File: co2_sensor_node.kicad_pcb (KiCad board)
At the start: 4 copper layers, 52.5 x 96 mm, 77 parts, among them J1 Conn_01x07_Female, J10 Conn_01x02_Male, J11 Conn_01x02_Male, J12 Conn_01x02_Male, J13 Conn_01x02_Male, J14 Conn_01x02, J15 Conn_01x06_Male, J2 Conn_01x04_Female, J3 Conn_01x07_Female, J4 Conn_01x04_Female, J5 Conn_01x04_Female, J6 TF-15x15, J7 SMA Female, J8 Conn_01x02_Male, J9 Conn_01x02_Male, Q1 AO3400A, Q2 AO3401A, Q3 AO3400A, Q4 AO3401A, Q5 AO3401A, SW1 K2-1102SP-C4SC-04, U1 RFM95W-868S2, U2 ublox_SAM-M8Q, U3 TPS62130, U4 TPS62130, U5 ESP32-WROOM-32D

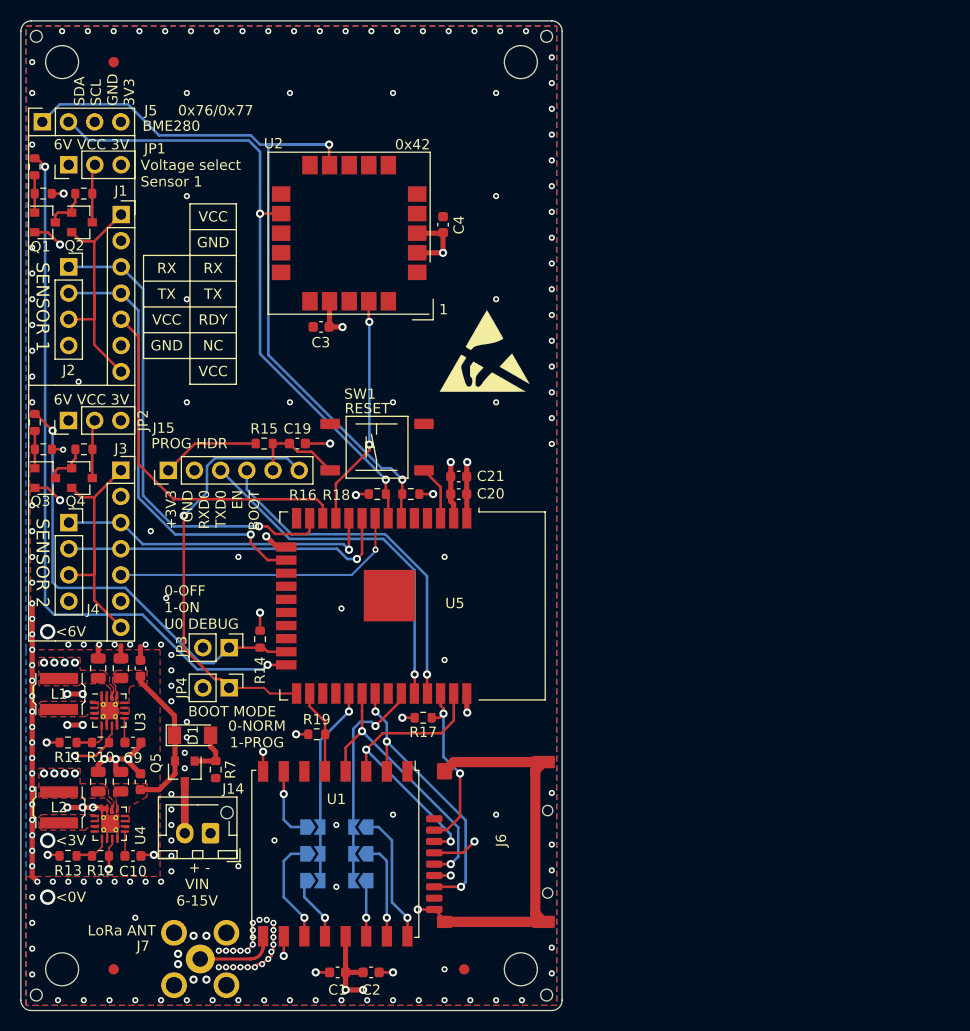
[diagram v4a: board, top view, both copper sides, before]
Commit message: Finish routing of Rev 1
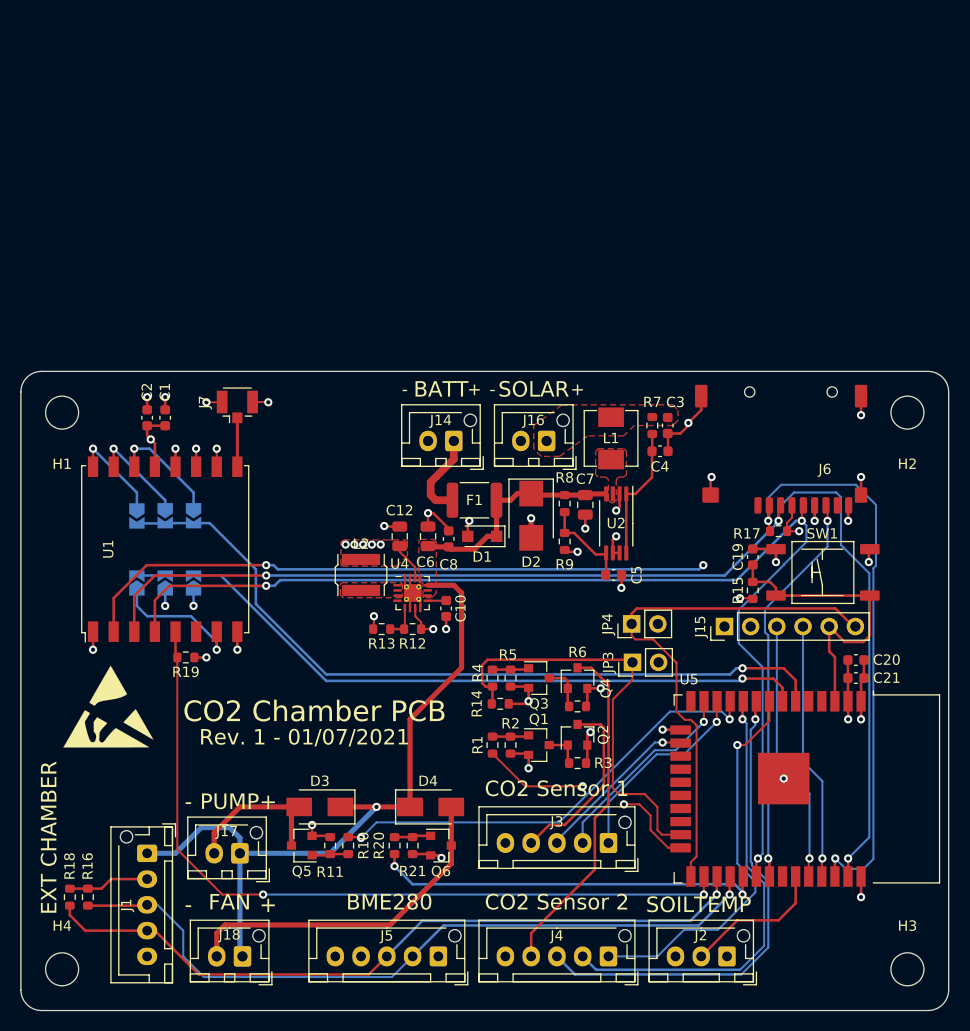
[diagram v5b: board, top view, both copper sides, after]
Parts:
- removed BOARD_FIDUCIAL (x3): Fiducial_1mm_Mask2mm, Fiducial:Fiducial_1mm_Mask2mm
- removed C11: 22u, Capacitor_SMD:C_0805_2012Metric
- removed C9: 3n3, Capacitor_SMD:C_0603_1608Metric
- removed JP1, JP2: PWR_JP, Connector_PinHeader_2.54mm:PinHeader_1x03_P2.54mm_Vertical
- removed the REF** at (171.5, 45.5)
- removed the REF** at (122.0, 138.5)
- removed the REF** at (122.0, 45.5)
- removed the REF** at (171.5, 138.5)
- removed U3: TPS62130, Package_DFN_QFN:VQFN-16-1EP_3x3mm_P0.5mm_EP1.68x1.68mm_ThermalVias
- added D2: P6SMB6.8CA, Diode_SMD:D_SMB, F.Cu at (170.0, 92.0)
- added D3: SS34, Diode_SMD:D_SMA, F.Cu at (149.5, 120.2)
- added D4: SS34, Diode_SMD:D_SMA, F.Cu at (160.2, 120.2)
- added F1: mSMD200-16V, Fuse:Fuse_1812_4532Metric, F.Cu at (164.5, 90.5)
- added J16: Conn_01x02, Connector_JST:JST_XH_B2B-XH-AM_1x02_P2.50mm_Vertical, F.Cu at (171.5, 84.8)
- added J17: Conn_01x02, Connector_JST:JST_XH_B2B-XH-AM_1x02_P2.50mm_Vertical, F.Cu at (141.8, 124.8)
- added J18: Conn_01x02, Connector_JST:JST_XH_B2B-XH-AM_1x02_P2.50mm_Vertical, F.Cu at (142.0, 134.8)
- added Q6: AO3400A, Package_TO_SOT_SMD:SOT-23, F.Cu at (161.2, 124.0)
- added R20: 220R, Resistor_SMD:R_0603_1608Metric, F.Cu at (156.8, 124.0)
- added R21: 10K, Resistor_SMD:R_0603_1608Metric, F.Cu at (158.5, 124.0)
- added R8: 820k, Resistor_SMD:R_0603_1608Metric, F.Cu at (173.2, 90.8)
- added R9: 360k, Resistor_SMD:R_0603_1608Metric, F.Cu at (173.2, 94.5)
- C4: value 100n -> 1n
- C5: value 10u -> 1n; footprint Capacitor_SMD:C_0805_2012Metric -> Capacitor_SMD:C_0603_1608Metric
- C7: value 100n -> 10u; footprint Capacitor_SMD:C_0603_1608Metric -> Capacitor_SMD:C_0805_2012Metric
- D1: value 5V6 -> SM4007PL; footprint Diode_SMD:D_MiniMELF -> Diode_SMD:D_SOD-123F
- J1, J3: value Conn_01x07_Female -> Conn_01x05; footprint Connector_PinSocket_2.54mm:PinSocket_1x07_P2.54mm_Vertical -> Connector_JST:JST_XH_B5B-XH-AM_1x05_P2.50mm_Vertical
- J2: value Conn_01x04_Female -> Conn_01x03; footprint Connector_PinSocket_2.54mm:PinSocket_1x04_P2.54mm_Vertical -> Connector_JST:JST_XH_B3B-XH-AM_1x03_P2.50mm_Vertical
- J4, J5: value Conn_01x04_Female -> Conn_01x05; footprint Connector_PinSocket_2.54mm:PinSocket_1x04_P2.54mm_Vertical -> Connector_JST:JST_XH_B5B-XH-AM_1x05_P2.50mm_Vertical
- J7: value SMA Female -> U.FL; footprint co2_sensor_node:TE_5-1814832-2_C482015 -> Connector_Coaxial:U.FL_Hirose_U.FL-R-SMT-1_Vertical
- L1: value 2u2 -> 10u; footprint co2_sensor_node:WPN4020 -> co2_sensor_node:MWSA0503S
- Q5: value AO3401A -> AO3400A
- R10: value 1M17 -> 220R
- R11: value 180k -> 10K
- R7: value 10k -> 1k
- U2: value ublox_SAM-M8Q -> SPV1040; footprint RF_GPS:ublox_SAM-M8Q -> Package_SO:TSSOP-8_4.4x3mm_P0.65mm
- moved J2 92.5 mm to (189.0, 134.8), turned to 180 degrees
- moved J5 89.6 mm to (161.0, 134.8), turned to 180 degrees
- moved H3 82.0 mm to (206.5, 136.0)
- moved R3 73.1 mm to (174.5, 116.0)
- moved R1 71.5 mm to (166.2, 114.2), turned to 90 degrees
- moved R2 70.1 mm to (168.0, 114.2), turned to 270 degrees
- moved Q1 69.8 mm to (170.8, 114.2)
- moved Q2 69.1 mm to (174.5, 113.2), turned to 90 degrees
- moved J4 67.2 mm to (177.5, 134.8), turned to 180 degrees
- moved J1 62.0 mm to (132.8, 124.8), turned to 270 degrees
- moved L1 59.7 mm to (177.8, 84.5), turned to 270 degrees
- moved J3 59.5 mm to (177.5, 123.8), turned to 180 degrees
- moved C2 58.0 mm to (132.8, 82.5), turned to 90 degrees
- moved C1 56.3 mm to (134.5, 82.5), turned to 90 degrees
- moved J15 56.0 mm to (188.8, 102.8)
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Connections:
- C3 pad 1: +3V3 -> Net-(C3-Pad1)
- C4 pad 1: +3V3 -> Net-(C4-Pad1)
- C5 pad 1: +BATT -> Net-(C5-Pad1)
- D1 pad 2: Net-(D1-Pad2) -> GND
- J1 pad 1: /CO2 Sensor Connector 1/VCC -> +BATT
- J1 pad 2: GND -> +3V3
- J1 pad 3: /Microprocessor section/UART1_RX -> /Microprocessor section/I2C_SCL
- J1 pad 4: /Microprocessor section/UART1_TX -> /Microprocessor section/I2C_SDA
- J1 pad 5: /CO2 Sensor Connector 1/N_RDY -> GND
- J14 pad 1: GND -> Net-(F1-Pad2)
- J14 pad 2: Net-(J14-Pad2) -> GND
- J2 pad 1: /Microprocessor section/UART1_RX -> +3V3
- J2 pad 2: /Microprocessor section/UART1_TX -> /Microprocessor section/TEMPSENSOR
- J2 pad 3: /CO2 Sensor Connector 1/VCC -> GND
- J3 pad 1: /CO2 Sensor Connector 2/VCC -> /CO2 Sensor Connector 1/N_RDY
- J3 pad 2: GND -> /Microprocessor section/UART1_RX
- J3 pad 3: /Microprocessor section/UART2_RX -> /Microprocessor section/UART1_TX
- J3 pad 4: /Microprocessor section/UART2_TX -> /CO2 Sensor Connector 1/VCC
- J3 pad 5: /CO2 Sensor Connector 2/N_RDY -> GND
- J4 pad 1: /Microprocessor section/UART2_RX -> /CO2 Sensor Connector 2/N_RDY
- J4 pad 2: /Microprocessor section/UART2_TX -> /Microprocessor section/UART2_RX
- J4 pad 3: /CO2 Sensor Connector 2/VCC -> /Microprocessor section/UART2_TX
- J4 pad 4: GND -> /CO2 Sensor Connector 2/VCC
- J5 pad 1: /Microprocessor section/I2C_SDA -> +3V3
- J5 pad 3: GND -> /Microprocessor section/I2C_SDA
- J5 pad 4: +3V3 -> GND
- L1 pad 1: Net-(L1-Pad1) -> Net-(C3-Pad1)
- L1 pad 2: +6V -> Net-(L1-Pad2)
- Q2 pad 2: /CO2 Sensor Connector 1/VCC -> +3V3
- Q2 pad 3: Net-(JP1-Pad2) -> /CO2 Sensor Connector 1/VCC
- Q4 pad 2: /CO2 Sensor Connector 2/VCC -> +3V3
- Q4 pad 3: Net-(JP2-Pad2) -> /CO2 Sensor Connector 2/VCC
- Q5 pad 1: Net-(D1-Pad2) -> Net-(Q5-Pad1)
- Q5 pad 2: +BATT -> GND
- Q5 pad 3: Net-(J14-Pad2) -> Net-(D3-Pad2)
- R10 pad 1: +6V -> Net-(Q5-Pad1)
- R10 pad 2: Net-(R10-Pad2) -> /Microprocessor section/PUMP_EN
- R11 pad 1: Net-(R10-Pad2) -> Net-(Q5-Pad1)
- R3 pad 1: Net-(JP1-Pad2) -> +3V3
- R6 pad 1: Net-(JP2-Pad2) -> +3V3
- R7 pad 1: Net-(D1-Pad2) -> Net-(C3-Pad1)
- R7 pad 2: GND -> Net-(C4-Pad1)
- U2 pad 1: GND -> Net-(C4-Pad1)
- U2 pad 2: +3V3 -> GND
- U2 pad 3: +3V3 -> Net-(L1-Pad2)
- U2 pad 4: GND -> +BATT
- U2 pad 5: GND -> Net-(C5-Pad1)
- U2 pad 7: Net-(U2-Pad7) -> GND
- U2 pad 8: Net-(U2-Pad8) -> Net-(C4-Pad1)
- U5 pad 11: /GNSS/ENABLE -> /Microprocessor section/PUMP_EN
- U5 pad 27: Net-(U5-Pad27) -> /Microprocessor section/I2C_SDA
- U5 pad 28: Net-(U5-Pad28) -> /Microprocessor section/I2C_SCL
- U5 pad 29: /LoRa Transceiver/IRQ1 -> /Fan/FAN
- U5 pad 33: /LoRa Transceiver/IRQ2 -> /Microprocessor section/TEMPSENSOR
- U5 pad 6: /Microprocessor section/I2C_SDA -> /LoRa Transceiver/IRQ2
- U5 pad 7: /Microprocessor section/I2C_SCL -> /LoRa Transceiver/IRQ1
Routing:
- net /LoRa Transceiver/MOSI: track 28.3 -> 117.5 mm, vias 2 -> 3
- net /LoRa Transceiver/MISO: track 28.1 -> 115.4 mm, vias 3 -> 4
- net /LoRa Transceiver/SCLK: track 26.9 -> 109.2 mm, vias 2 -> 3
- net +BATT: track 14.8 -> 92.5 mm, vias 0 -> 1
- net +6V: track 72.5 -> 0.00 mm, vias 6 -> 0
- net /LoRa Transceiver/CSN: track 8.16 -> 75.8 mm, vias 0 -> 2
- net GND: track 144.2 -> 81.5 mm, vias 207 -> 34
- net /LoRa Transceiver/IRQ2: track 21.5 -> 74.7 mm
- net /LoRa Transceiver/IRQ1: track 19.3 -> 68.6 mm
- net /CO2 Sensor Connector 1/ENABLE: track 70.1 -> 22.9 mm
- net /Microprocessor section/PUMP_EN: track 0.00 -> 44.2 mm, vias 0 -> 2
- net /SD Card/CSN: track 17.1 -> 57.3 mm
- net /Fan/FAN: track 0.00 -> 38.0 mm, vias 0 -> 2
- net Net-(D4-Pad2): track 0.00 -> 33.1 mm
- net /Microprocessor section/UART1_RX: track 47.2 -> 19.8 mm
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- added copper zone on F.Cu, net Net-(C3-Pad1)
- added copper zone on F.Cu, net Net-(L1-Pad2)
- removed copper zone on F.Cu, net +6V
- removed copper zone on B.Cu, net GND
- removed copper zone on F.Cu, net GND
- removed copper zone on F.Cu, net Net-(L1-Pad1)
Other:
- board size 52.5 x 96 mm -> 90 x 62 mm
- board text added: "+"
- board text added: "-"
- board text added: "BATT"
- board text added: "CO2 Chamber PCB"
- board text added: "CO2 Sensor 1"
- board text added: "CO2 Sensor 2"
- board text added: "EXT CHAMBER"
- board text added: "FAN"
- board text added: "PUMP"
- board text added: "Rev. 1 - 01/07/2021"
- board text added: "SOILTEMP"
- board text added: "SOLAR"
- board text removed: "+ - VIN 6-15V"
- board text removed: "+3V3 GND RXD0 TXD0 EN BOOT"
- board text removed: "0-NORM 1-PROG"
- board text removed: "0-OFF 1-ON U0 DEBUG"
- board text removed: "0x42"
- board text removed: "0x76/0x77"
- board text removed: "1"
- board text removed: "6V VCC 3V"
- board text removed: "<0V"
- board text removed: "<3V"
- board text removed: "<6V"
- board text removed: "BOARD STACKUP: JLC7628"
- board text removed: "BOOT MODE"
- board text removed: "DIO2 DIO1 DIO0"
- board text removed: "DIO5 DIO3 DIO4"
- board text removed: "GND"
- board text removed: "IRQ1"
- board text removed: "IRQ2"
- board text removed: "LoRa ANT"
- board text removed: "NC"
- board text removed: "RDY"
- board text removed: "RESET"
- board text removed: "RX"
- board text removed: "SDA SCL GND 3V3"
- board text removed: "SENSOR 1"
- board text removed: "SENSOR 2"
- board text removed: "TX"
- board text removed: "VCC"
- board text removed: "Voltage select Sensor 1"

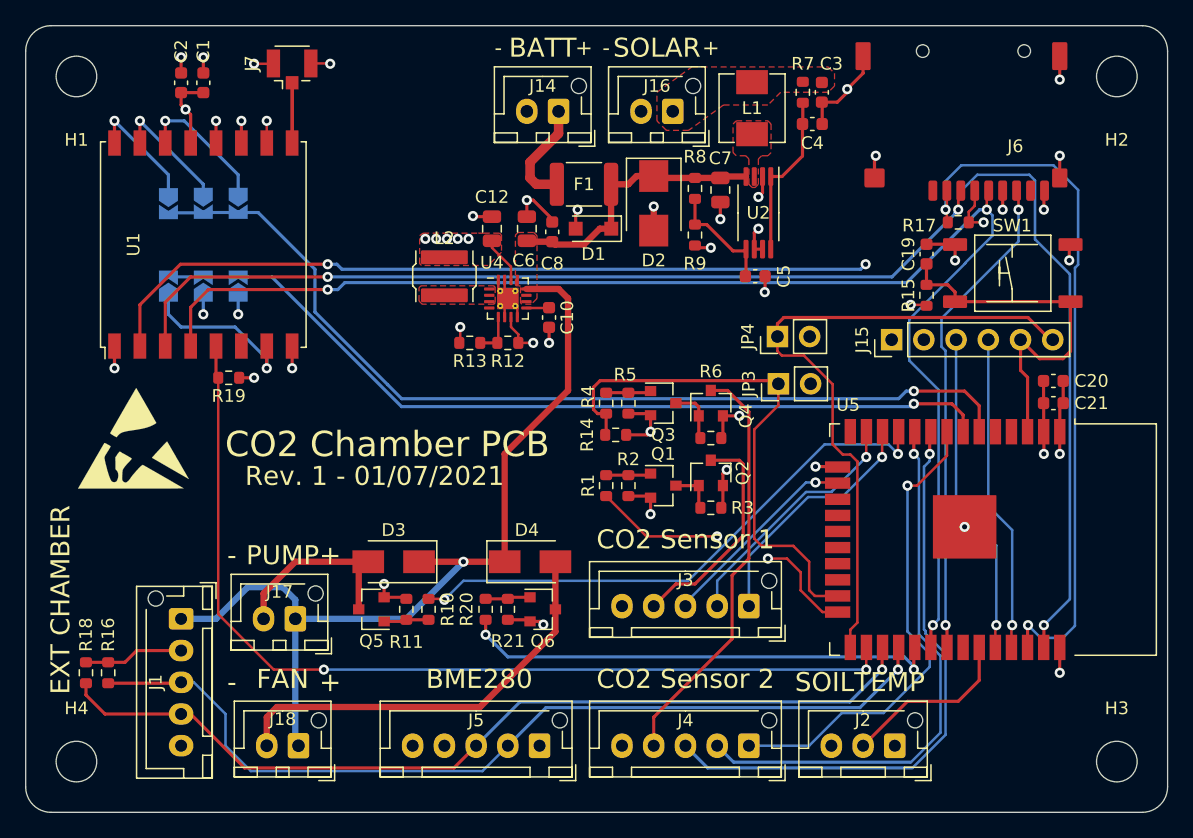
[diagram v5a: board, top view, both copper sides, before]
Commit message: Remove unused circuits
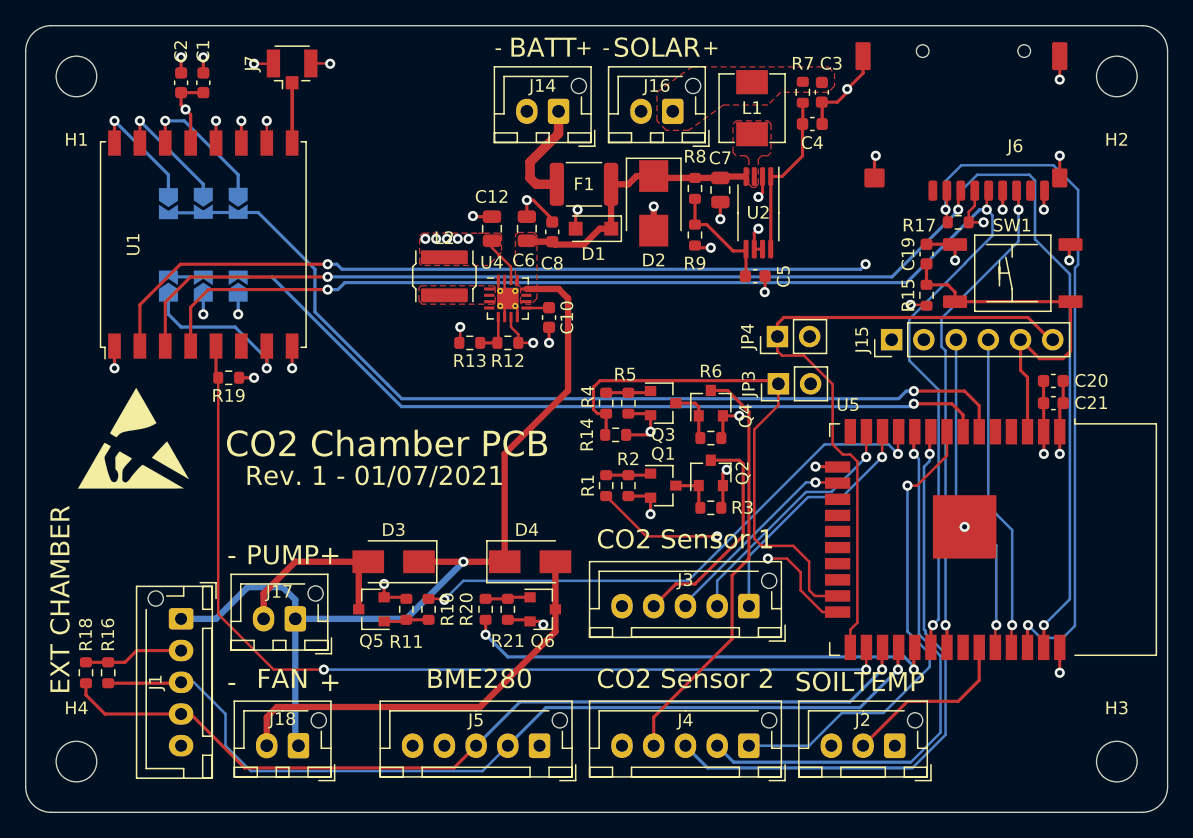
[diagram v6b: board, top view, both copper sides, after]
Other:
- net class Default removed

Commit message: Finalize schematic
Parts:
- removed C19, C21: 100n, Capacitor_SMD:C_0603_1608Metric
- removed C20: 1u, Capacitor_SMD:C_0603_1608Metric
- removed D4: SS34, Diode_SMD:D_SMA
- removed J14, J16, J17, J18: Conn_01x02, Connector_JST:JST_XH_B2B-XH-AM_1x02_P2.50mm_Vertical
- removed J15: Conn_01x06_Male, Connector_PinHeader_2.54mm:PinHeader_1x06_P2.54mm_Vertical
- removed JP3: MTDO_JP, Connector_PinHeader_2.54mm:PinHeader_1x02_P2.54mm_Vertical
- removed JP4: BOOT_JP, Connector_PinHeader_2.54mm:PinHeader_1x02_P2.54mm_Vertical
- removed L2: 2u2, co2_sensor_node:WPN4020
- removed Q5, Q6: AO3400A, Package_TO_SOT_SMD:SOT-23
- removed R17, R19: 10k, Resistor_SMD:R_0603_1608Metric
- removed R18: 4k7, Resistor_SMD:R_0603_1608Metric
- removed R20: 220R, Resistor_SMD:R_0603_1608Metric
- removed R21: 10K, Resistor_SMD:R_0603_1608Metric
- removed REF**: ESD-Logo_8.9x8mm_SilkScreen, Symbol:ESD-Logo_8.9x8mm_SilkScreen
- removed U4: TPS62130, Package_DFN_QFN:VQFN-16-1EP_3x3mm_P0.5mm_EP1.68x1.68mm_ThermalVias
- removed U5: ESP32-WROOM-32D, RF_Module:ESP32-WROOM-32
- added C11: 10u, Capacitor_SMD:C_0805_2012Metric, F.Cu at (210.5, 99.8)
- added C9: 100n, Capacitor_SMD:C_0603_1608Metric, F.Cu at (117.7, 55.7)
- added JP1: MTDO_JP, Connector_PinHeader_2.54mm:PinHeader_1x02_P2.54mm_Vertical, F.Cu at (113.3, 56.8)
- added JP2: BOOT_JP, Connector_PinHeader_2.54mm:PinHeader_1x02_P2.54mm_Vertical, F.Cu at (108.7, 81.2)
- added TP1: 3V3_Switched, TestPoint:TestPoint_Loop_D2.50mm_Drill1.0mm_LowProfile, F.Cu at (106.9, 115.3)
- added TP10: GND, TestPoint:TestPoint_Loop_D2.50mm_Drill1.0mm_LowProfile, F.Cu at (118.3, 106.9)
- added TP11: GND, TestPoint:TestPoint_Loop_D2.50mm_Drill1.0mm_LowProfile, F.Cu at (125.5, 102.3)
- added TP12: TEMP_SENSOR, TestPoint:TestPoint_Loop_D2.50mm_Drill1.0mm_LowProfile, F.Cu at (106.9, 119.9)
- added TP13: MOISTURE_SENSOR, TestPoint:TestPoint_Loop_D2.50mm_Drill1.0mm_LowProfile, F.Cu at (113.7, 110.2)
- added TP14: CELL_1, TestPoint:TestPoint_Loop_D2.50mm_Drill1.0mm_LowProfile, F.Cu at (216.3, 62.1)
- added TP15: CELL_2, TestPoint:TestPoint_Loop_D2.50mm_Drill1.0mm_LowProfile, F.Cu at (225.9, 56.8)
- added TP16: VALVE_1_REV, TestPoint:TestPoint_Loop_D2.50mm_Drill1.0mm_LowProfile, F.Cu at (200.8, 112.3)
- added TP17: VALVE_2_FWD, TestPoint:TestPoint_Loop_D2.50mm_Drill1.0mm_LowProfile, F.Cu at (209.4, 96.0)
- added TP18: VALVE_1_FWD, TestPoint:TestPoint_Loop_D2.50mm_Drill1.0mm_LowProfile, F.Cu at (209.4, 91.3)
- added TP19: VALVE_2_REV, TestPoint:TestPoint_Loop_D2.50mm_Drill1.0mm_LowProfile, F.Cu at (214.0, 91.3)
- added TP2: SCL, TestPoint:TestPoint_Loop_D2.50mm_Drill1.0mm_LowProfile, F.Cu at (120.9, 97.6)
- added TP20: MOSI, TestPoint:TestPoint_Loop_D2.50mm_Drill1.0mm_LowProfile, F.Cu at (170.2, 70.3)
- added TP21: SCLK, TestPoint:TestPoint_Loop_D2.50mm_Drill1.0mm_LowProfile, F.Cu at (174.8, 70.3)
- added TP22: SD_CSN, TestPoint:TestPoint_Loop_D2.50mm_Drill1.0mm_LowProfile, F.Cu at (187.9, 56.8)
- added TP23: MISO, TestPoint:TestPoint_Loop_D2.50mm_Drill1.0mm_LowProfile, F.Cu at (170.2, 74.9)
- added TP3: SDA, TestPoint:TestPoint_Loop_D2.50mm_Drill1.0mm_LowProfile, F.Cu at (112.9, 105.6)
- added TP4: 3V3, TestPoint:TestPoint_Loop_D2.50mm_Drill1.0mm_LowProfile, F.Cu at (123.0, 106.9)
- added TP5: PWR_EN, TestPoint:TestPoint_Loop_D2.50mm_Drill1.0mm_LowProfile, F.Cu at (109.0, 110.2)
- added TP6: CO2_RX, TestPoint:TestPoint_Loop_D2.50mm_Drill1.0mm_LowProfile, F.Cu at (111.6, 114.9)
- added TP7: CO2_TX, TestPoint:TestPoint_Loop_D2.50mm_Drill1.0mm_LowProfile, F.Cu at (118.3, 111.6)
- added TP8: GND, TestPoint:TestPoint_Loop_D2.50mm_Drill1.0mm_LowProfile, F.Cu at (125.5, 97.6)
- added TP9: GND, TestPoint:TestPoint_Loop_D2.50mm_Drill1.0mm_LowProfile, F.Cu at (120.9, 102.3)
- added U3: TC1508S, Package_SO:SOP-16_3.9x9.9mm_P1.27mm, F.Cu at (202.8, 94.7)
- C1: value 1u -> 10u; footprint Capacitor_SMD:C_0603_1608Metric -> Capacitor_SMD:C_0805_2012Metric
- C10: value 3n3 -> 220u; footprint Capacitor_SMD:C_0603_1608Metric -> Capacitor_THT:CP_Radial_D8.0mm_P3.50mm
- C12: value 22u -> 100n; footprint Capacitor_SMD:C_0805_2012Metric -> Capacitor_SMD:C_0603_1608Metric
- C3: value 1u -> 3n3
- C4, C5: value 1n -> 1u
- C6: value 10u -> 22u
- C7: value 10u -> 100n; footprint Capacitor_SMD:C_0805_2012Metric -> Capacitor_SMD:C_0603_1608Metric
- C8: value 100n -> 1u
- D1: value SM4007PL -> Green LED; footprint Diode_SMD:D_SOD-123F -> LED_SMD:LED_0603_1608Metric
- D2: value P6SMB6.8CA -> ZMM5V6-M; footprint Diode_SMD:D_SMB -> Diode_SMD:D_MiniMELF
- J1: value Conn_01x05 -> Conn_01x03; footprint Connector_JST:JST_XH_B5B-XH-AM_1x05_P2.50mm_Vertical -> Connector_PinSocket_2.54mm:PinSocket_1x03_P2.54mm_Vertical
- J10, J9: value Conn_01x02_Male -> Conn_01x05; footprint Jumper:SolderJumper-2_P1.3mm_Open_TrianglePad1.0x1.5mm -> Connector_JST:JST_XH_B5B-XH-AM_1x05_P2.50mm_Vertical; moved to F.Cu
- J11: value Conn_01x02_Male -> Conn_01x06_Male; footprint Jumper:SolderJumper-2_P1.3mm_Open_TrianglePad1.0x1.5mm -> Connector_PinHeader_2.54mm:PinHeader_1x06_P2.54mm_Vertical; moved to F.Cu
- J12: value Conn_01x02_Male -> Conn_01x02; footprint Jumper:SolderJumper-2_P1.3mm_Open_TrianglePad1.0x1.5mm -> co2_sensor_node:KF301-5.0-2P; moved to F.Cu
- J13: value Conn_01x02_Male -> TF-15x15; footprint Jumper:SolderJumper-2_P1.3mm_Open_TrianglePad1.0x1.5mm -> co2_sensor_node:TF-15x15; moved to F.Cu
- J2: footprint Connector_JST:JST_XH_B3B-XH-AM_1x03_P2.50mm_Vertical -> Connector_PinSocket_2.54mm:PinSocket_1x03_P2.54mm_Vertical
- J3, J4: value Conn_01x05 -> Conn_01x02; footprint Connector_JST:JST_XH_B5B-XH-AM_1x05_P2.50mm_Vertical -> co2_sensor_node:KF301-5.0-2P
- J5: value Conn_01x05 -> Conn_01x03; footprint Connector_JST:JST_XH_B5B-XH-AM_1x05_P2.50mm_Vertical -> co2_sensor_node:KF301-5.0-3P
- J6: value TF-15x15 -> Conn_01x03; footprint co2_sensor_node:TF-15x15 -> co2_sensor_node:KF301-5.0-3P
- J7: value U.FL -> Conn_01x02; footprint Connector_Coaxial:U.FL_Hirose_U.FL-R-SMT-1_Vertical -> Connector_JST:JST_XH_B2B-XH-AM_1x02_P2.50mm_Vertical
- J8: value Conn_01x02_Male -> Conn_01x03; footprint Jumper:SolderJumper-2_P1.3mm_Open_TrianglePad1.0x1.5mm -> Connector_JST:JST_XH_B3B-XH-AM_1x03_P2.50mm_Vertical; moved to F.Cu
- L1: value 10u -> 2u2; footprint co2_sensor_node:MWSA0503S -> co2_sensor_node:WPN4020
- Q3: value AO3400A -> AO3401A
- Q4: value AO3401A -> AO3400A
- R1: value 220 -> 4k7
- R10: value 220R -> 562k
- R11: value 10K -> 180k
- R12: value 562k -> 10k
- R13: value 180k -> 10k
- R14: value 10k -> 220R
- R15: value 10k -> 10K
- R16: value 4k7 -> 10k
- R2: value 10k -> 4k7
- R3: value 10k -> 1k
- R7: value 1k -> 220
- R8: value 820k -> 220
- R9: value 360k -> 1M
- U1: value RFM95W-868S2 -> TPS62130; footprint RF_Module:HOPERF_RFM9XW_SMD -> Package_DFN_QFN:VQFN-16-1EP_3x3mm_P0.5mm_EP1.68x1.68mm_ThermalVias
- U2: value SPV1040 -> ESP32-WROOM-32D; footprint Package_SO:TSSOP-8_4.4x3mm_P0.65mm -> RF_Module:ESP32-WROOM-32
- moved J6 112.2 mm to (80.2, 99.8), turned to 0 degrees
- moved H3 107.3 mm to (102.7, 109.0)
- moved J3 97.5 mm to (80.2, 118.4), turned to 0 degrees
- moved C7 96.4 mm to (78.8, 90.8), turned to 0 degrees
- moved U1 94.5 mm to (220.9, 57.1), turned to 0 degrees
- moved H2 93.5 mm to (114.6, 99.3)
- moved R3 92.0 mm to (82.9, 124.5), turned to 0 degrees
- moved D1 91.6 mm to (78.9, 124.5), turned to 0 degrees
- moved R16 91.5 mm to (187.5, 60.4), turned to 0 degrees
- moved J2 88.8 mm to (108.3, 97.6), turned to 0 degrees
- moved SW1 88.7 mm to (107.8, 73.1)
- moved U2 88.3 mm to (91.6, 76.0), turned to 0 degrees
- moved J4 87.3 mm to (97.5, 99.8), turned to 0 degrees
- moved C2 84.9 mm to (216.0, 65.6), turned to 0 degrees
- moved J5 84.8 mm to (80.2, 109.1), turned to 0 degrees
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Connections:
- C1 pad 1: +3V3 -> +BATT
- C10 pad 1: Net-(C10-Pad1) -> /Atmo sensor/3V3_IN
- C12 pad 1: +3V3 -> /Atmo sensor/3V3_IN
- C2 pad 1: +3V3 -> +BATT
- C4 pad 1: Net-(C4-Pad1) -> /Microprocessor section/CELL_1
- C5 pad 1: Net-(C5-Pad1) -> /Microprocessor section/CELL_2
- C6 pad 1: +BATT -> +3V3
- C7 pad 1: +BATT -> /Microprocessor section/EN
- C8 pad 1: +BATT -> +3V3
- D1 pad 1: +BATT -> GND
- D1 pad 2: GND -> Net-(D1-Pad2)
- D2 pad 2: GND -> Net-(D2-Pad2)
- D3 pad 1: +BATT -> /Atmo sensor/3V3_IN
- F1 pad 1: +BATT -> Net-(F1-Pad1)
- J1 pad 1: +BATT -> /Atmo sensor/3V3_IN
- J1 pad 2: +3V3 -> /Microprocessor section/MOISTURE_SENSOR
- J1 pad 3: /Microprocessor section/I2C_SCL -> GND
- J10 pad 1: Net-(J10-Pad1) -> /Atmo sensor/3V3_IN
- J10 pad 2: /LoRa Transceiver/IRQ2 -> /Atmo sensor/SCL
- J11 pad 1: Net-(J11-Pad1) -> +3V3
- J11 pad 2: /LoRa Transceiver/IRQ1 -> GND
- J12 pad 1: Net-(J12-Pad1) -> /Atmo sensor/3V3_IN
- J12 pad 2: /LoRa Transceiver/IRQ2 -> Net-(D3-Pad2)
- J13 pad 1: Net-(J13-Pad1) -> unconnected-(J13-Pad1)
- J13 pad 2: /LoRa Transceiver/IRQ1 -> /Microprocessor section/SPI_SD_CSN
- J2 pad 1: +3V3 -> /Atmo sensor/3V3_IN
- J2 pad 2: /Microprocessor section/TEMPSENSOR -> /Microprocessor section/TEMP_SENSOR
- J3 pad 1: /CO2 Sensor Connector 1/N_RDY -> /Valve Driver/OUT_A
- J3 pad 2: /Microprocessor section/UART1_RX -> /Valve Driver/OUT_B
- J4 pad 1: /CO2 Sensor Connector 2/N_RDY -> /Valve Driver/OUT_C
- J4 pad 2: /Microprocessor section/UART2_RX -> /Valve Driver/OUT_D
- J5 pad 1: +3V3 -> /Atmo sensor/3V3_IN
- J5 pad 2: /Microprocessor section/I2C_SCL -> /Microprocessor section/MOISTURE_SENSOR
- J5 pad 3: /Microprocessor section/I2C_SDA -> GND
- J6 pad 1: Net-(J6-Pad1) -> /Atmo sensor/3V3_IN
- J6 pad 2: /SD Card/CSN -> /Microprocessor section/TEMP_SENSOR
- J6 pad 3: /LoRa Transceiver/MOSI -> GND
- J7 pad 1: Net-(J7-Pad1) -> Net-(F1-Pad2)
- J8 pad 2: /LoRa Transceiver/IRQ2 -> Net-(J8-Pad2)
- J9 pad 1: Net-(J9-Pad1) -> unconnected-(J9-Pad1)
- J9 pad 2: /LoRa Transceiver/IRQ1 -> /CO2 Sensor Connector/UART_TX
- L1 pad 1: Net-(C3-Pad1) -> Net-(L1-Pad1)
- L1 pad 2: Net-(L1-Pad2) -> +3V3
- Q2 pad 3: /CO2 Sensor Connector 1/VCC -> /Atmo sensor/3V3_IN
- Q3 pad 1: Net-(Q3-Pad1) -> Net-(D2-Pad2)
- Q3 pad 2: GND -> +BATT
- Q3 pad 3: Net-(Q3-Pad3) -> Net-(F1-Pad1)
- Q4 pad 1: Net-(Q3-Pad3) -> Net-(Q4-Pad1)
- Q4 pad 2: +3V3 -> GND
- Q4 pad 3: /CO2 Sensor Connector 2/VCC -> Net-(D3-Pad2)
- R1 pad 1: /CO2 Sensor Connector 1/ENABLE -> /Atmo sensor/SCL
- R1 pad 2: Net-(Q1-Pad1) -> /Atmo sensor/3V3_IN
- R10 pad 1: Net-(Q5-Pad1) -> +3V3
- R10 pad 2: /Microprocessor section/PUMP_EN -> Net-(R10-Pad2)
- R11 pad 1: Net-(Q5-Pad1) -> Net-(R10-Pad2)
- R12 pad 1: +3V3 -> GND
- R12 pad 2: Net-(R12-Pad2) -> /Microprocessor section/MTDO
- R13 pad 1: Net-(R12-Pad2) -> +3V3
- R13 pad 2: GND -> /Microprocessor section/EN
- R14 pad 1: GND -> Net-(Q4-Pad1)
- R14 pad 2: /CO2 Sensor Connector 2/ENABLE -> /Fan/FAN
- R15 pad 1: +3V3 -> Net-(Q4-Pad1)
- R15 pad 2: /Microprocessor section/EN -> GND
- R16 pad 1: +3V3 -> /Atmo sensor/3V3_IN
- R16 pad 2: /Microprocessor section/I2C_SCL -> /Microprocessor section/SPI_SD_CSN
- R2 pad 1: Net-(Q1-Pad1) -> /Atmo sensor/SDA
- R2 pad 2: GND -> /Atmo sensor/3V3_IN
- R3 pad 1: +3V3 -> Net-(D1-Pad2)
- R3 pad 2: Net-(Q1-Pad3) -> /Microprocessor section/STATUS_LED
- R4 pad 1: /CO2 Sensor Connector 2/ENABLE -> /Microprocessor section/PWR_EN
- R4 pad 2: Net-(Q3-Pad1) -> Net-(Q1-Pad1)
- R5 pad 1: Net-(Q3-Pad1) -> Net-(Q1-Pad1)
- R6 pad 2: Net-(Q3-Pad3) -> Net-(Q1-Pad3)
- R7 pad 1: Net-(C3-Pad1) -> Net-(J8-Pad2)
- R7 pad 2: Net-(C4-Pad1) -> /Microprocessor section/CELL_1
- R8 pad 1: +BATT -> Net-(J8-Pad1)
- R8 pad 2: Net-(C5-Pad1) -> /Microprocessor section/CELL_2
- R9 pad 1: Net-(C5-Pad1) -> Net-(D2-Pad2)
- U1 pad 1: GND -> Net-(L1-Pad1)
- U1 pad 10: GND -> +BATT
- U1 pad 11: Net-(J13-Pad1) -> +BATT
- U1 pad 12: Net-(J11-Pad1) -> +BATT
- U1 pad 13: +3V3 -> +BATT
- U1 pad 14: Net-(J8-Pad1) -> +3V3
- U1 pad 15: Net-(J10-Pad1) -> GND
- U1 pad 16: Net-(J12-Pad1) -> GND
- U1 pad 2: /LoRa Transceiver/MISO -> Net-(L1-Pad1)
- U1 pad 3: /LoRa Transceiver/MOSI -> Net-(L1-Pad1)
- U1 pad 4: /LoRa Transceiver/SCLK -> unconnected-(U1-Pad4)
- U1 pad 5: /LoRa Transceiver/CSN -> Net-(R10-Pad2)
- U1 pad 6: Net-(U1-Pad6) -> GND
- U1 pad 7: Net-(J9-Pad1) -> +3V3
- U1 pad 9: Net-(J7-Pad1) -> Net-(C3-Pad1)
- U2 pad 1: Net-(C4-Pad1) -> GND
- U2 pad 2: GND -> +3V3
- U2 pad 3: Net-(L1-Pad2) -> /Microprocessor section/EN
- U2 pad 4: +BATT -> unconnected-(U2-Pad4)
- U2 pad 5: Net-(C5-Pad1) -> unconnected-(U2-Pad5)
- U2 pad 6: GND -> /Microprocessor section/CELL_1
- U2 pad 7: GND -> /Microprocessor section/CELL_2
- U2 pad 8: Net-(C4-Pad1) -> /Microprocessor section/VALVE_1_REV
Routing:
- net /LoRa Transceiver/MOSI: track 117.5 -> 0.00 mm, vias 3 -> 0
- net /LoRa Transceiver/MISO: track 115.4 -> 0.00 mm, vias 4 -> 0
- net /LoRa Transceiver/SCLK: track 109.2 -> 0.00 mm, vias 3 -> 0
- net +BATT: track 92.5 -> 0.00 mm, vias 1 -> 0
- net GND: track 81.5 -> 0.00 mm, vias 34 -> 0
- net /LoRa Transceiver/CSN: track 75.8 -> 0.00 mm, vias 2 -> 0
- net /LoRa Transceiver/IRQ2: track 74.7 -> 0.00 mm, vias 1 -> 0
- net /Microprocessor section/I2C_SCL: track 71.7 -> 0.00 mm, vias 1 -> 0
- net /Microprocessor section/I2C_SDA: track 71.0 -> 0.00 mm, vias 1 -> 0
- net /LoRa Transceiver/IRQ1: track 68.6 -> 0.00 mm, vias 1 -> 0
- net /SD Card/CSN: track 57.3 -> 0.00 mm, vias 2 -> 0
- net /Microprocessor section/BOOT: track 52.3 -> 0.00 mm
- net /Microprocessor section/UART2_TX: track 47.1 -> 0.00 mm, vias 1 -> 0
- net /Microprocessor section/PUMP_EN: track 44.2 -> 0.00 mm, vias 2 -> 0
- net /Microprocessor section/UART2_RX: track 43.7 -> 0.00 mm, vias 1 -> 0
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- removed copper zone on F.Cu, net +3V3
- removed copper zone on In2.Cu, net +3V3
- removed copper zone on F.Cu, net +BATT
- removed copper zone on F.Cu, net Net-(C3-Pad1)
- removed copper zone on F.Cu, net Net-(L1-Pad2)
- removed copper zone on F.Cu, net Net-(L2-Pad1)
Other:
- board outline removed
- board text removed: "+"
- board text removed: "-"
- board text removed: "BATT"
- board text removed: "BME280"
- board text removed: "CO2 Chamber PCB"
- board text removed: "CO2 Sensor 1"
- board text removed: "CO2 Sensor 2"
- board text removed: "EXT CHAMBER"
- board text removed: "FAN"
- board text removed: "PUMP"
- board text removed: "Rev. 1 - 01/07/2021"
- board text removed: "SOILTEMP"
- board text removed: "SOLAR"
